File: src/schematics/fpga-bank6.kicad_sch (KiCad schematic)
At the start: 7 parts

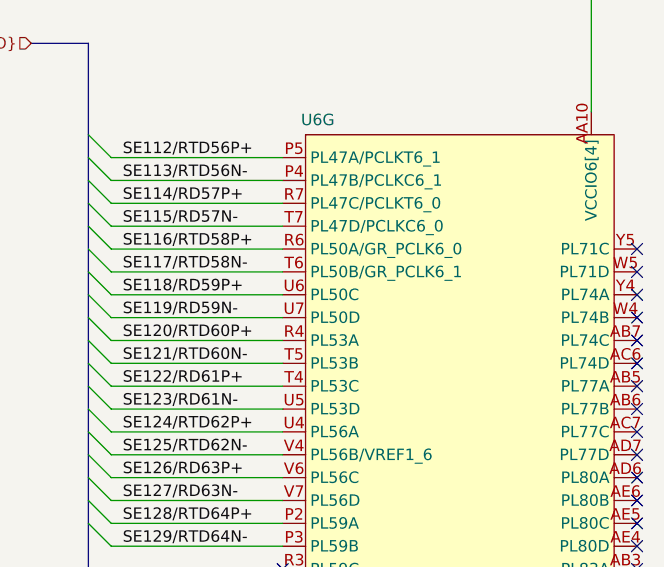
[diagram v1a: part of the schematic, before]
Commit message: ✅ Validate the schematic symbols (#33)
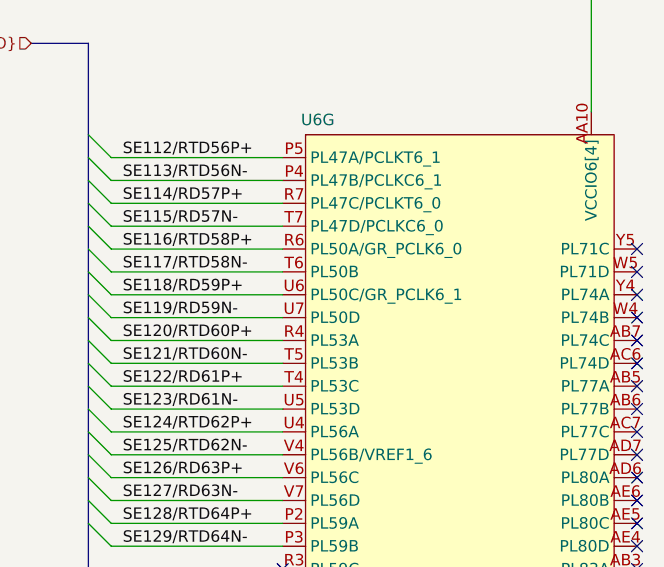
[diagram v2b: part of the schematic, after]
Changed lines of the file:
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@@
 		(pin "AA11"
+		)
+		(pin "AG24"
+		)
+		(pin "AC29"
+		)
+		(pin "AC4"
+		)
+		(pin "AE26"
+		)
+		(pin "AE7"
+		)
+		(pin "AG2"
+		)
+		(pin "AG31"
+		)
+		(pin "AK10"
+		)
+		(pin "AK12"
+		)
+		(pin "AK13"
+		)
+		(pin "AK15"
+		)
+		(pin "AK16"
+		)
+		(pin "AK18"
+		)
+		(pin "AK19"
+		)
+		(pin "AK21"
+		)
+		(pin "AK22"
+		)
+		(pin "AK24"
+		)
+		(pin "AK25"
+		)
+		(pin "AK9"
+		)
+		(pin "E26"
+		)
+		(pin "E7"
+		)
+		(pin "G10"
+		)
+		(pin "G11"
+		)
+		(pin "G14"
+		)
+		(pin "G15"
+		)
+		(pin "G16"
+		)
+		(pin "G17"
+		)
+		(pin "G18"
+		)
+		(pin "G19"
+		)
+		(pin "G22"
+		)
+		(pin "G23"
+		)
+		(pin "G24"
+		)
+		(pin "G9"
+		)
+		(pin "H29"
+		)
+		(pin "H4"
+		)
+		(pin "L28"
+		)
+		(pin "L5"
+		)
+		(pin "P20"
+		)
+		(pin "R11"
+		)
+		(pin "V3"
+		)
+		(pin "V30"
+		)
+		(pin "W27"
+		)
+		(pin "W6"
+		)
+		(pin "AG5"
+		)
+		(pin "AJ5"
+		)
+		(pin "AK5"
+		)
+		(pin "AM5"
 		)
 		(instances

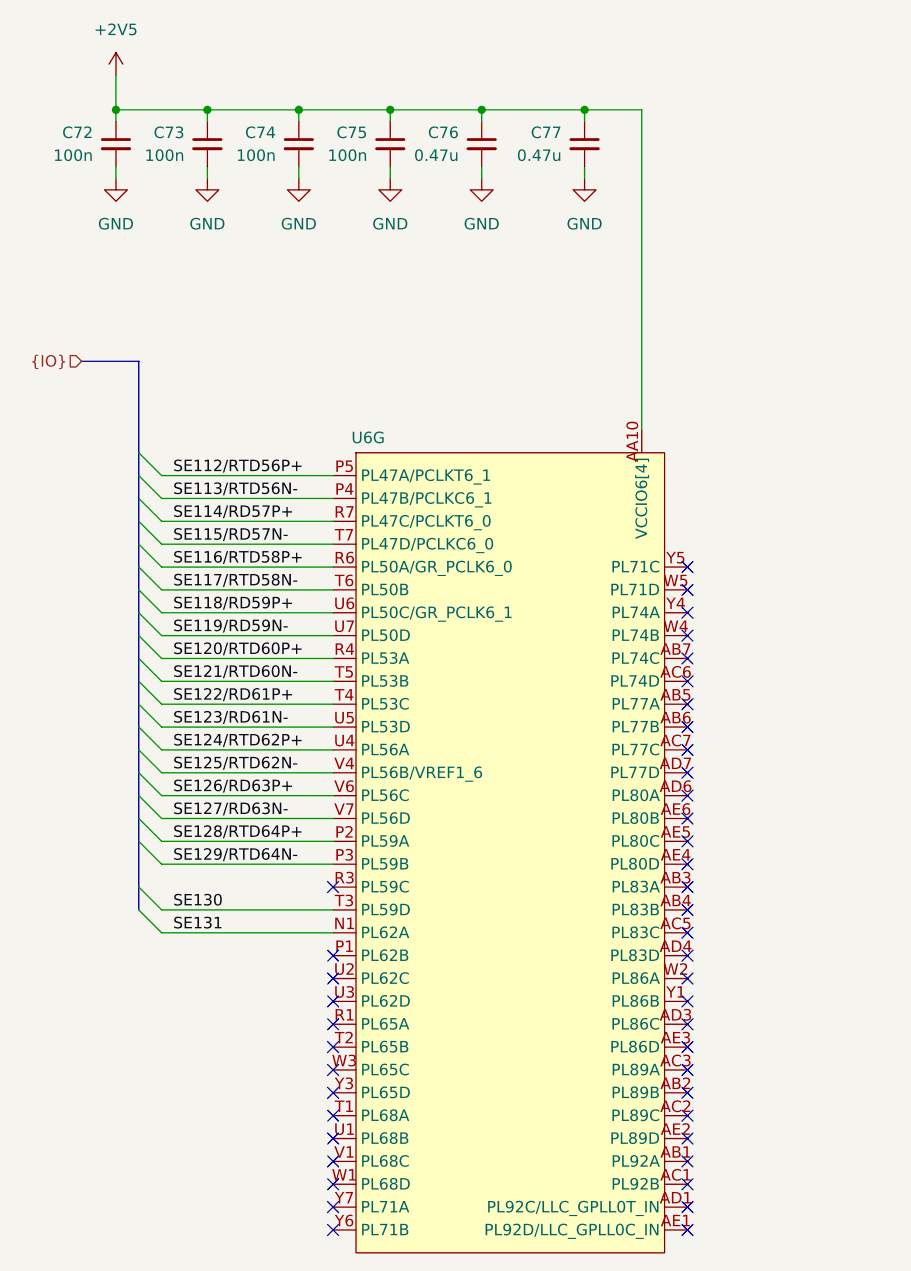
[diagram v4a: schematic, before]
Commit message: ✨ Replace some LVDS diff pairs with 3v3 single-ended signals (#56)
* ✨ Replace some LVDS diff pairs with 3v3 single-ended signals

* Finishes replacing LVDS diff pairs with 3v3 single ended
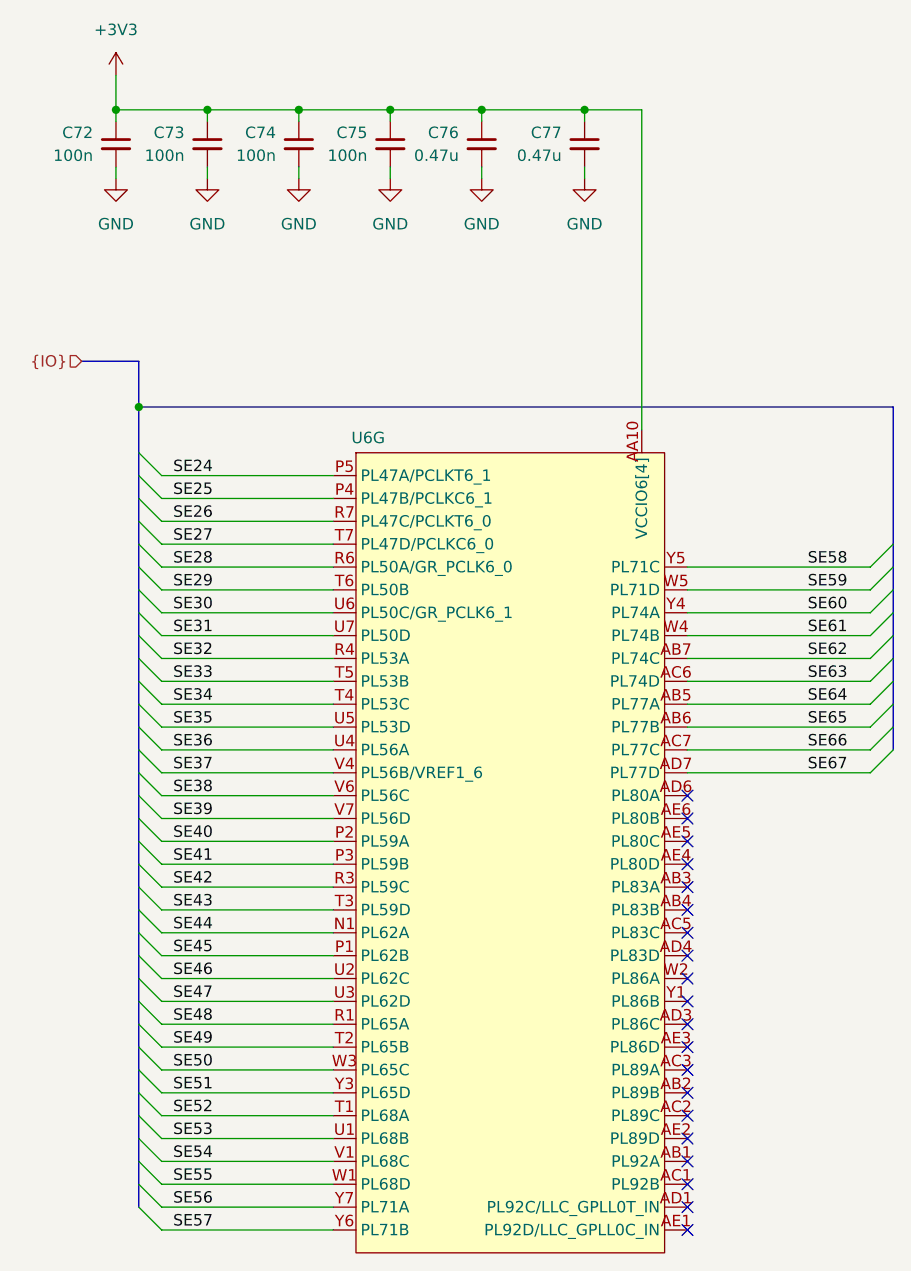
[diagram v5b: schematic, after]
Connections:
- net SE64: now reaches U6.AB5 (PL77A)
- net SE65: now reaches U6.AB6 (PL77B)
- net SE62: now reaches U6.AB7 (PL74C)
- net SE63: now reaches U6.AC6 (PL74D)
- net SE66: now reaches U6.AC7 (PL77C)
- net SE67: now reaches U6.AD7 (PL77D)
- net SE45: now reaches U6.P1 (PL62B)
- net SE48: now reaches U6.R1 (PL65A)
- net SE42: now reaches U6.R3 (PL59C)
- net SE52: now reaches U6.T1 (PL68A)
- net SE49: now reaches U6.T2 (PL65B)
- net SE53: now reaches U6.U1 (PL68B)
- net SE46: now reaches U6.U2 (PL62C)
- net SE47: now reaches U6.U3 (PL62D)
- net SE54: now reaches U6.V1 (PL68C)
- net SE55: now reaches U6.W1 (PL68D)
- net SE50: now reaches U6.W3 (PL65C)
- net SE61: now reaches U6.W4 (PL74B)
- net SE59: now reaches U6.W5 (PL71D)
- net SE51: now reaches U6.Y3 (PL65D)
- net SE60: now reaches U6.Y4 (PL74A)
- net SE58: now reaches U6.Y5 (PL71C)
- net SE57: now reaches U6.Y6 (PL71B)
- net SE56: now reaches U6.Y7 (PL71A)
- net +2V5 renamed +3V3
- net SE112/RTD56P+ renamed SE24
- net SE113/RTD56N- renamed SE25
- net SE114/RD57P+ renamed SE26
- net SE115/RD57N- renamed SE27
- net SE116/RTD58P+ renamed SE28
- net SE117/RTD58N- renamed SE29
- net SE118/RD59P+ renamed SE30
- net SE119/RD59N- renamed SE31
- net SE120/RTD60P+ renamed SE32
- net SE121/RTD60N- renamed SE33
- net SE122/RD61P+ renamed SE34
- net SE123/RD61N- renamed SE35
- net SE124/RTD62P+ renamed SE36
- net SE125/RTD62N- renamed SE37
- net SE126/RD63P+ renamed SE38
- net SE127/RD63N- renamed SE39
- net SE128/RTD64P+ renamed SE40
- net SE129/RTD64N- renamed SE41
- net SE130 renamed SE43
- net SE131 renamed SE44
- no-connect marks 44 -> 20

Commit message: Add footprint for ecp5 (#75)
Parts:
- U6: footprint (none) -> ECAP5-DPROC:LFE5U-85F-_BG756C
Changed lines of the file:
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@@
 			)
 		)
-		(property "Footprint" ""
+		(property "Footprint" "ECAP5-DPROC:LFE5U-85F-_BG756C"
 			(at 147.32 72.39 0)
 			(effects

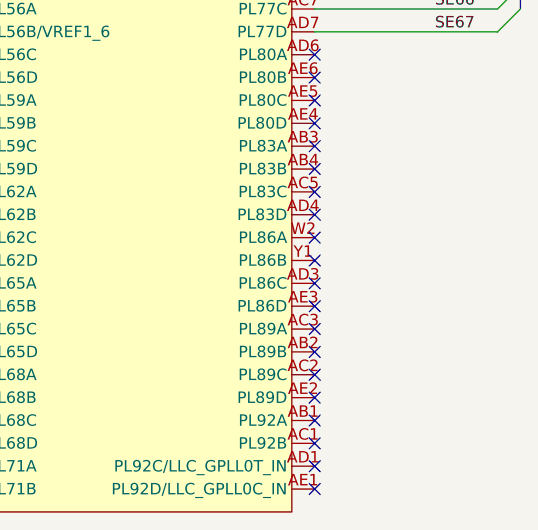
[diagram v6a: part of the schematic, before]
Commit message: Add footprint for the io connector
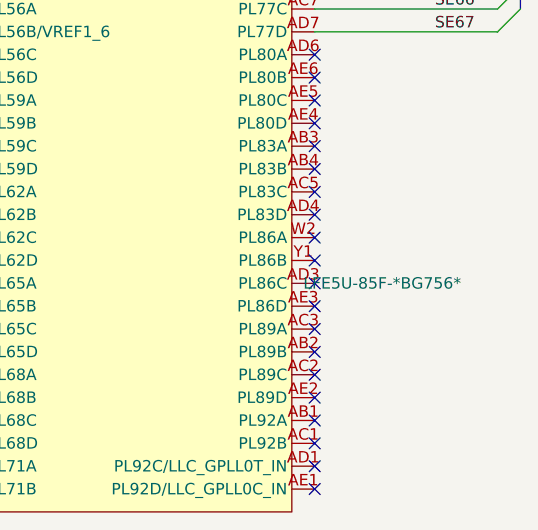
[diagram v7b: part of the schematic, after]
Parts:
- U6: value ~ -> LFE5U-85F-*BG756*
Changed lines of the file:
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@@
 			)
 		)
-		(property "Value" "~"
+		(property "Value" "LFE5U-85F-*BG756*"
 			(at 180.34 133.35 0)
 			(effects

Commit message: Add remaining component footprints (#79)
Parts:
- C72, C73, C74, C75, C76, C77: footprint (none) -> Capacitor_SMD:C_0402_1005Metric
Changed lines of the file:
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@@
 			)
 		)
-		(property "Footprint" ""
+		(property "Footprint" "Capacitor_SMD:C_0402_1005Metric"
 			(at 148.59 35.56 0)
 			(effects
@@
 			)
 		)
-		(property "Footprint" ""
+		(property "Footprint" "Capacitor_SMD:C_0402_1005Metric"
 			(at 118.11 35.56 0)
 			(effects
@@
 			)
 		)
-		(property "Footprint" ""
+		(property "Footprint" "Capacitor_SMD:C_0402_1005Metric"
 			(at 128.27 35.56 0)
 			(effects
@@
 			)
 		)
-		(property "Footprint" ""
+		(property "Footprint" "Capacitor_SMD:C_0402_1005Metric"
 			(at 158.75 35.56 0)
 			(effects
@@
 			)
 		)
-		(property "Footprint" ""
+		(property "Footprint" "Capacitor_SMD:C_0402_1005Metric"
 			(at 138.43 35.56 0)
 			(effects
@@
 			)
 		)
-		(property "Footprint" ""
+		(property "Footprint" "Capacitor_SMD:C_0402_1005Metric"
 			(at 170.18 35.56 0)
 			(effects
